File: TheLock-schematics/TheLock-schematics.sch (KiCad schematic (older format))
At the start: 4 parts

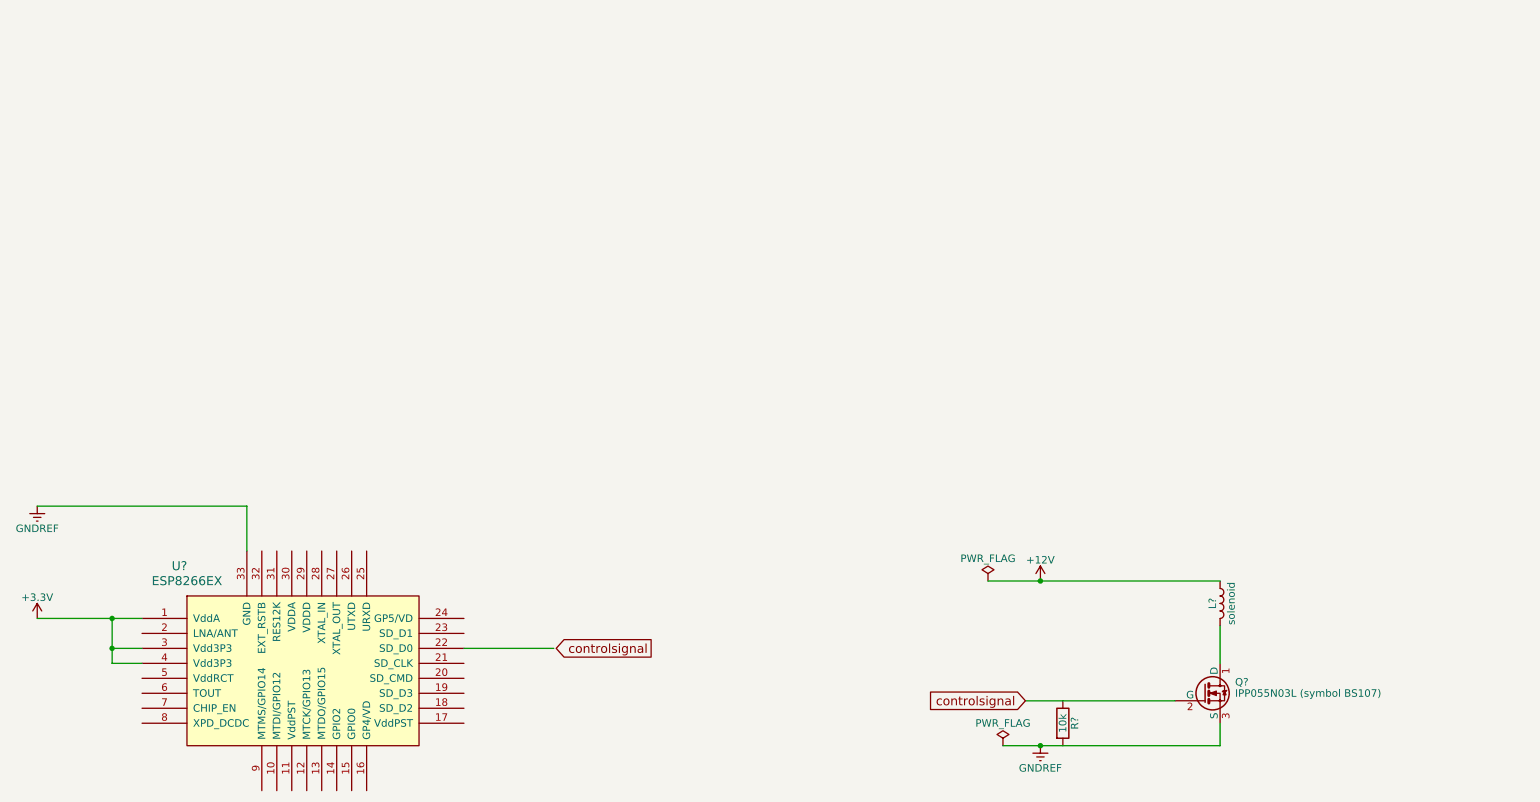
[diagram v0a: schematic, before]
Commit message: schematics: Add optical key sensor
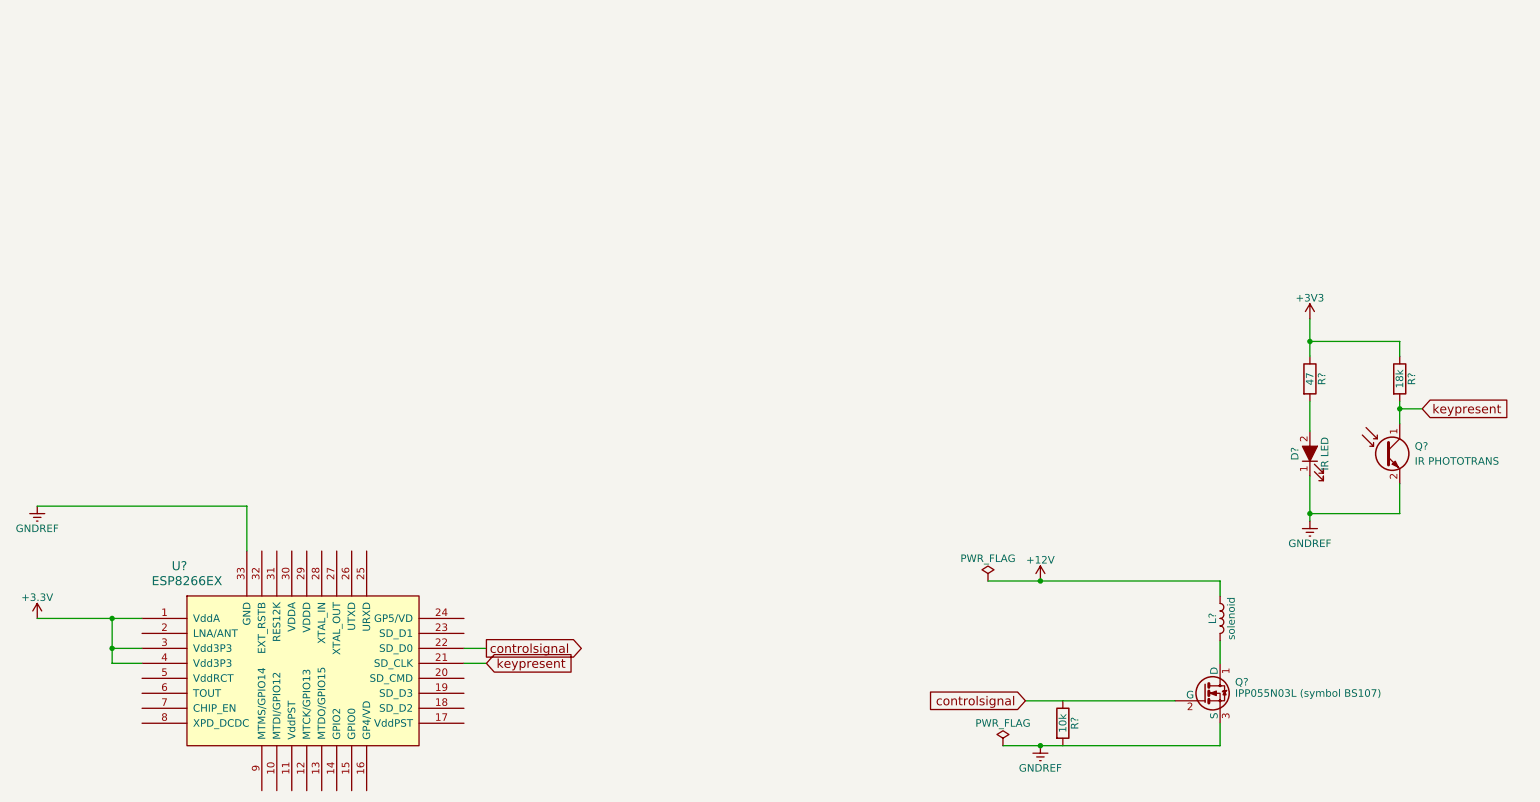
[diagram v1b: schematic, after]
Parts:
- added D?: IR LED, symbol LED_ALT
- added Q?: IR PHOTOTRANS, symbol Q_Photo_NPN
- added R?: 47, symbol R
- added R?: 18k, symbol R
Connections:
- net labels added: +3V3, keypresent
- wire segments 12 -> 31
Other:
- moved on the sheet: L?
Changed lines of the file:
@@
 LIBS:contrib
 LIBS:valves
-LIBS:ESP8266
 LIBS:TheLock-schematics-cache
 EELAYER 25 0
@@
 	9200 5700 9200 5550
 Wire Wire Line
-	7750 5700 9200 5700
+	7750 5700 8000 5700
+Wire Wire Line
+	8000 5700 9200 5700
 $Comp
 L L L?
 U 1 1 5957E9AE
-P 9200 4750
-F 0 "L?" V 9150 4750 50  0000 C CNN
-F 1 "solenoid" V 9275 4750 50  0000 C CNN
-F 2 "" H 9200 4750 50  0001 C CNN
-F 3 "" H 9200 4750 50  0001 C CNN
-	1    9200 4750
-	1    0    0    -1
-$EndComp
-Wire Wire Line
-	9200 5150 9200 4900
-Wire Wire Line
-	7650 4600 9200 4600
+P 9200 4850
+F 0 "L?" V 9150 4850 50  0000 C CNN
+F 1 "solenoid" V 9275 4850 50  0000 C CNN
+F 2 "" H 9200 4850 50  0001 C CNN
+F 3 "" H 9200 4850 50  0001 C CNN
+	1    9200 4850
+	1    0    0    -1
+$EndComp
+Wire Wire Line
+	9200 5150 9200 5000
+Wire Wire Line
+	7650 4600 8000 4600
+Wire Wire Line
+	8000 4600 9200 4600
 Text GLabel 7900 5400 0    60   Input ~ 0
 controlsignal
@@
 	1    0    0    -1
 $EndComp
-Text GLabel 5400 5050 0    60   Output ~ 0
+Text GLabel 4300 5050 2    60   Output ~ 0
 controlsignal
 Wire Wire Line
-	4750 5050 4150 5050
+	4300 5050 4150 5050
 $Comp
 L GNDREF #PWR?
@@
 $EndComp
 Wire Wire Line
-	1300 4850 2000 4850
+	1300 4850 1800 4850
+Wire Wire Line
+	1800 4850 2000 4850
 Wire Wire Line
 	2000 5050 1800 5050
 Wire Wire Line
-	1800 4850 1800 5150
+	1800 4850 1800 5050
+Wire Wire Line
+	1800 5050 1800 5150
 Connection ~ 1800 4850
 Wire Wire Line
 	1800 5150 2000 5150
 Connection ~ 1800 5050
+$Comp
+L LED_ALT D?
+U 1 1 595B8197
+P 9800 3750
+F 0 "D?" H 9800 3850 50  0000 C CNN
+F 1 "IR LED" H 9800 3650 50  0000 C CNN
+F 2 "" H 9800 3750 50  0001 C CNN
+F 3 "" H 9800 3750 50  0001 C CNN
+	1    9800 3750
+	0    -1   -1   0
+$EndComp
+$Comp
+L +3V3 #PWR?
+U 1 1 595B83C2
+P 9800 2850
+F 0 "#PWR?" H 9800 2700 50  0001 C CNN
+F 1 "+3V3" H 9800 2990 50  0000 C CNN
+F 2 "" H 9800 2850 50  0001 C CNN
+F 3 "" H 9800 2850 50  0001 C CNN
+	1    9800 2850
+	1    0    0    -1
+$EndComp
+$Comp
+L Q_Photo_NPN Q?
+U 1 1 595B83E5
+P 10300 3750
+F 0 "Q?" H 10500 3800 50  0000 L CNN
+F 1 "IR PHOTOTRANS" H 10500 3700 50  0000 L CNN
+F 2 "" H 10500 3850 50  0001 C CNN
+F 3 "" H 10300 3750 50  0001 C CNN
+	1    10300 3750
+	1    0    0    -1
+$EndComp
+Wire Wire Line
+	10400 4150 9800 4150
+$Comp
+L GNDREF #PWR?
+U 1 1 595B863D
+P 9800 4200
+F 0 "#PWR?" H 9800 3950 50  0001 C CNN
+F 1 "GNDREF" H 9800 4050 50  0000 C CNN
+F 2 "" H 9800 4200 50  0001 C CNN
+F 3 "" H 9800 4200 50  0001 C CNN
+	1    9800 4200
+	1    0    0    -1
+$EndComp
+Connection ~ 9800 4150
+Wire Wire Line
+	10400 4150 10400 3950
+Wire Wire Line
+	10400 3000 9800 3000
+Connection ~ 9800 3000
+$Comp
+L R R?
+U 1 1 595B89FB
+P 9800 3250
+F 0 "R?" V 9880 3250 50  0000 C CNN
+F 1 "47" V 9800 3250 50  0000 C CNN
+F 2 "" V 9730 3250 50  0001 C CNN
+F 3 "" H 9800 3250 50  0001 C CNN
+	1    9800 3250
+	1    0    0    -1
+$EndComp
+$Comp
+L R R?
+U 1 1 595B8B72
+P 10400 3250
+F 0 "R?" V 10480 3250 50  0000 C CNN
+F 1 "18k" V 10400 3250 50  0000 C CNN
+F 2 "" V 10330 3250 50  0001 C CNN
+F 3 "" H 10400 3250 50  0001 C CNN
+	1    10400 3250
+	1    0    0    -1
+$EndComp
+Wire Wire Line
+	10400 3100 10400 3000
+Wire Wire Line
+	10400 3400 10400 3450
+Wire Wire Line
+	10400 3450 10400 3550
+Wire Wire Line
+	9800 3400 9800 3600
+Wire Wire Line
+	9800 3900 9800 4150
+Wire Wire Line
+	9800 4150 9800 4200
+Wire Wire Line
+	9800 2850 9800 3000
+Wire Wire Line
+	9800 3000 9800 3100
+Text GLabel 10550 3450 2    60   Input ~ 0
+keypresent
+Wire Wire Line
+	10400 3450 10550 3450
+Connection ~ 10400 3450
+Wire Wire Line
+	9200 4600 9200 4700
+Text GLabel 4300 5150 2    60   Input ~ 0
+keypresent
+Wire Wire Line
+	4150 5150 4300 5150
+Wire Wire Line
+	4300 5150 4300 5150
 $EndSCHEMATC

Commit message: electronics: Update to the lock driver board
Will have header connectors, so that 3-4 of them
can be connected to a single ESP8266 module
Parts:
- removed L?: solenoid, symbol L
- removed U?: ESP8266EX, symbol ESP8266EX
- added D?: LED, symbol LED
- added J? (x2): Conn_01x04, symbol Conn_01x04
- added J?: Conn_01x02_Female, symbol Conn_01x02_Female
- added J?: Conn_01x02_Male, symbol Conn_01x02_Male
- added R?: R, symbol R
- Q?: value IPP055N03L (symbol BS107) -> IPP055N03L; footprint TO_SOT_Packages_THT:TO-92_Molded_Narrow -> TO_SOT_Packages_THT:TO-220_Horizontal; symbol BS107 -> BS107-RESCUE-TheLock-schematics
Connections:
- net controlsignal is gone; now on net unlock: Q?.2 (G)
- net +12V: now also J?.2 (Pin_2), J?.3 (Pin_3)
- net +3V3: now also J?.1 (Pin_1)
- net GNDREF: now also R?.2, D?.1 (K), J?.2 (Pin_2); no longer D?.1 (K)
- net keypresent: now also J?.2 (Pin_2)
- net solenoid-: now reaches Q?.1 (D)
- net solenoid-: now also J?.4 (Pin_4)
- net unlock: now reaches R?.1
- net unlock: now also J?.4 (Pin_4)
- net at D?.2 (A): now also J?.1 (Pin_1); no longer R?.2
- new net: D?.1 (K), J?.2 (Pin_2)
- new net: J?.1 (Pin_1), R?.2
- new net: D?.2 (A), R?.2
- new net GNDPWR: J?.1 (Pin_1)
- new net status: J?.3 (Pin_3), R?.1
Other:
- moved on the sheet: D?, Q?, R?

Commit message: electronics: Rough layout of lock board
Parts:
- D1: renamed from D?; footprint (none) -> LEDs:LED_0805_HandSoldering
- D2: renamed from D?; footprint (none) -> LEDs:LED_1206_HandSoldering
- J1: renamed from J?; value Conn_01x04 -> CONN_SIGNAL; footprint (none) -> Pin_Headers:Pin_Header_Angled_1x04_Pitch2.54mm
- J2: renamed from J?; value Conn_01x04 -> CONN_POWER; footprint (none) -> Pin_Headers:Pin_Header_Angled_1x04_Pitch2.54mm
- J3: renamed from J?; value Conn_01x02_Female -> CONN_IRBOARD; footprint (none) -> Socket_Strips:Socket_Strip_Angled_1x02_Pitch2.54mm
- J4: renamed from J?; value Conn_01x02_Male -> CONN_IRLED; footprint (none) -> Pin_Headers:Pin_Header_Angled_1x02_Pitch2.54mm
- Q1: renamed from Q?; value IPP055N03L -> PMV20XNE; footprint TO_SOT_Packages_THT:TO-220_Horizontal -> TO_SOT_Packages_SMD:SOT-23W_Handsoldering; symbol BS107-RESCUE-TheLock-schematics -> Q_NMOS_GSD
- Q2: renamed from Q?; footprint (none) -> Diodes_SMD:D_0805
- R1, R2, R3, R4: renamed from R?; footprint (none) -> Resistors_SMD:R_1210_HandSoldering
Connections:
- net GNDPWR: now also D2.1 (K), J3.2 (Pin_2), Q1.2 (S), Q2.2 (E), R1.2
- net solenoid-: now also Q1.3 (D); no longer Q1.1 (D)
- net unlock: now also Q1.1 (G); no longer Q1.2 (G)
- removed net GNDREF: D2.1 (K), J3.2 (Pin_2), Q1.3 (S), Q2.2 (E), R1.2
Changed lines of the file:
@@
 $EndDescr
 $Comp
-L GNDREF #PWR?
+L GNDREF #PWR01
 U 1 1 5957DA2E
 P 8700 3850
-F 0 "#PWR?" H 8700 3600 50  0001 C CNN
+F 0 "#PWR01" H 8700 3600 50  0001 C CNN
 F 1 "GNDREF" H 8700 3700 50  0000 C CNN
 F 2 "" H 8700 3850 50  0001 C CNN
@@
 $EndComp
 $Comp
-L +12V #PWR?
+L +12V #PWR02
 U 1 1 5957DA45
 P 8700 2800
-F 0 "#PWR?" H 8700 2650 50  0001 C CNN
+F 0 "#PWR02" H 8700 2650 50  0001 C CNN
 F 1 "+12V" H 8700 2940 50  0000 C CNN
 F 2 "" H 8700 2800 50  0001 C CNN
@@
 $EndComp
 $Comp
-L BS107-RESCUE-TheLock-schematics Q?
+L Q_NMOS_GSD Q1
 U 1 1 5957E897
 P 8600 3400
-F 0 "Q?" H 8800 3475 50  0000 L CNN
-F 1 "IPP055N03L" H 8800 3400 50  0000 L CNN
-F 2 "TO_SOT_Packages_THT:TO-220_Horizontal" H 8800 3325 50  0001 L CIN
+F 0 "Q1" H 8800 3475 50  0000 L CNN
+F 1 "PMV20XNE" H 8800 3400 50  0000 L CNN
+F 2 "TO_SOT_Packages_SMD:SOT-23W_Handsoldering" H 8800 3325 50  0001 L CIN
 F 3 "" H 8600 3400 50  0001 L CNN
 	1    8600 3400
@@
 Wire Wire Line
 	8700 3800 8700 3850
-Text GLabel 8150 3450 0    60   Input ~ 0
+Text GLabel 8050 3400 0    60   Input ~ 0
 unlock
 Wire Wire Line
-	8150 3450 8300 3450
-Wire Wire Line
-	8300 3450 8400 3450
-$Comp
-L R R?
+	8050 3400 8300 3400
+Wire Wire Line
+	8300 3400 8400 3400
+$Comp
+L R R1
 U 1 1 5957EABF
 P 8300 3650
-F 0 "R?" V 8380 3650 50  0000 C CNN
+F 0 "R1" V 8380 3650 50  0000 C CNN
 F 1 "10k" V 8300 3650 50  0000 C CNN
-F 2 "" V 8230 3650 50  0001 C CNN
+F 2 "Resistors_SMD:R_1210_HandSoldering" V 8230 3650 50  0001 C CNN
 F 3 "" H 8300 3650 50  0001 C CNN
 	1    8300 3650
@@
 $EndComp
 $Comp
-L LED_ALT D?
+L LED_ALT D1
 U 1 1 595B8197
 P 9650 1900
-F 0 "D?" H 9650 2000 50  0000 C CNN
+F 0 "D1" H 9650 2000 50  0000 C CNN
 F 1 "IR LED" H 9650 1800 50  0000 C CNN
-F 2 "" H 9650 1900 50  0001 C CNN
+F 2 "LEDs:LED_0805_HandSoldering" H 9650 1900 50  0001 C CNN
 F 3 "" H 9650 1900 50  0001 C CNN
 	1    9650 1900
@@
 $EndComp
 $Comp
-L +3V3 #PWR?
+L +3V3 #PWR03
 U 1 1 595B83C2
 P 8750 1000
-F 0 "#PWR?" H 8750 850 50  0001 C CNN
+F 0 "#PWR03" H 8750 850 50  0001 C CNN
 F 1 "+3V3" H 8750 1140 50  0000 C CNN
 F 2 "" H 8750 1000 50  0001 C CNN
@@
 $EndComp
 $Comp
-L Q_Photo_NPN Q?
+L Q_Photo_NPN Q2
 U 1 1 595B83E5
 P 10150 1900
-F 0 "Q?" H 10350 1950 50  0000 L CNN
+F 0 "Q2" H 10350 1950 50  0000 L CNN
 F 1 "IR PHOTOTRANS" H 10350 1850 50  0000 L CNN
-F 2 "" H 10350 2000 50  0001 C CNN
+F 2 "Diodes_SMD:D_0805" H 10350 2000 50  0001 C CNN
 F 3 "" H 10150 1900 50  0001 C CNN
 	1    10150 1900
@@
 $EndComp
 $Comp
-L GNDREF #PWR?
+L GNDREF #PWR04
 U 1 1 595B863D
 P 8750 2250
-F 0 "#PWR?" H 8750 2000 50  0001 C CNN
+F 0 "#PWR04" H 8750 2000 50  0001 C CNN
 F 1 "GNDREF" H 8750 2100 50  0000 C CNN
 F 2 "" H 8750 2250 50  0001 C CNN
@@
 	10250 2100 10250 2250
 $Comp
-L R R?
+L R R2
 U 1 1 595B89FB
 P 8750 1300
-F 0 "R?" V 8830 1300 50  0000 C CNN
+F 0 "R2" V 8830 1300 50  0000 C CNN
 F 1 "47" V 8750 1300 50  0000 C CNN
-F 2 "" V 8680 1300 50  0001 C CNN
+F 2 "Resistors_SMD:R_1210_HandSoldering" V 8680 1300 50  0001 C CNN
 F 3 "" H 8750 1300 50  0001 C CNN
 	1    8750 1300
@@
 $EndComp
 $Comp
-L R R?
+L R R3
 U 1 1 595B8B72
 P 10250 1300
-F 0 "R?" V 10330 1300 50  0000 C CNN
+F 0 "R3" V 10330 1300 50  0000 C CNN
 F 1 "18k" V 10250 1300 50  0000 C CNN
-F 2 "" V 10180 1300 50  0001 C CNN
+F 2 "Resistors_SMD:R_1210_HandSoldering" V 10180 1300 50  0001 C CNN
 F 3 "" H 10250 1300 50  0001 C CNN
 	1    10250 1300
@@
 Connection ~ 10250 1550
 $Comp
-L Conn_01x04 J?
+L Conn_01x04 J2
 U 1 1 59CF7CC0
 P 7650 2000
-F 0 "J?" H 7650 2300 50  0000 C CNN
-F 1 "Conn_01x04" H 7650 1700 50  0000 C CNN
-F 2 "" H 7650 2000 50  0001 C CNN
+F 0 "J2" H 7650 2300 50  0000 C CNN
+F 1 "CONN_POWER" H 7650 1700 50  0000 C CNN
+F 2 "Pin_Headers:Pin_Header_Angled_1x04_Pitch2.54mm" H 7650 2000 50  0001 C CNN
 F 3 "" H 7650 2000 50  0001 C CNN
 	1    7650 2000
@@
 $EndComp
 $Comp
-L +12V #PWR?
+L +12V #PWR05
 U 1 1 59CF7D47
 P 7100 2000
-F 0 "#PWR?" H 7100 1850 50  0001 C CNN
+F 0 "#PWR05" H 7100 1850 50  0001 C CNN
 F 1 "+12V" H 7100 2140 50  0000 C CNN
 F 2 "" H 7100 2000 50  0001 C CNN
@@
 $EndComp
 $Comp
-L GNDPWR #PWR?
+L GNDPWR #PWR06
 U 1 1 59CF7EAE
 P 6900 1900
-F 0 "#PWR?" H 6900 1700 50  0001 C CNN
+F 0 "#PWR06" H 6900 1700 50  0001 C CNN
 F 1 "GNDPWR" H 6900 1770 50  0000 C CNN
 F 2 "" H 6900 1850 50  0001 C CNN
@@
 $EndComp
 Wire Wire Line
-	6900 1900 7450 1900
+	6900 1900 7300 1900
+Wire Wire Line
+	7300 1900 7450 1900
 Wire Wire Line
 	8750 1850 8750 1450
 $Comp
-L +3.3V #PWR?
+L +3.3V #PWR07
 U 1 1 59D38CF5
 P 10250 1000
-F 0 "#PWR?" H 10250 850 50  0001 C CNN
+F 0 "#PWR07" H 10250 850 50  0001 C CNN
 F 1 "+3.3V" H 10250 1140 50  0000 C CNN
 F 2 "" H 10250 1000 50  0001 C CNN
@@
 $EndComp
 $Comp
-L GNDREF #PWR?
+L GNDREF #PWR08
 U 1 1 59D38D56
 P 10250 2250
-F 0 "#PWR?" H 10250 2000 50  0001 C CNN
+F 0 "#PWR08" H 10250 2000 50  0001 C CNN
 F 1 "GNDREF" H 10250 2100 50  0000 C CNN
 F 2 "" H 10250 2250 50  0001 C CNN
@@
 Connection ~ 8700 3800
 Wire Wire Line
-	8300 3500 8300 3450
-Connection ~ 8300 3450
+	8300 3500 8300 3400
+Connection ~ 8300 3400
 Wire Wire Line
 	8700 3150 8800 3150
@@
 	8750 1950 8850 1950
 $Comp
-L Conn_01x02_Female J?
+L Conn_01x02_Female J3
 U 1 1 59D39A33
 P 9050 1850
-F 0 "J?" H 9050 1950 50  0000 C CNN
-F 1 "Conn_01x02_Female" H 9150 1650 50  0000 C CNN
-F 2 "" H 9050 1850 50  0001 C CNN
+F 0 "J3" H 9050 1950 50  0000 C CNN
+F 1 "CONN_IRBOARD" H 9150 1650 50  0000 C CNN
+F 2 "Socket_Strips:Socket_Strip_Angled_1x02_Pitch2.54mm" H 9050 1850 50  0001 C CNN
 F 3 "" H 9050 1850 50  0001 C CNN
 	1    9050 1850
@@
 $EndComp
 $Comp
-L Conn_01x02_Male J?
+L Conn_01x02_Male J4
 U 1 1 59D39A82
 P 9150 1850
-F 0 "J?" H 9150 1950 50  0000 C CNN
-F 1 "Conn_01x02_Male" H 9150 2050 50  0000 C CNN
-F 2 "" H 9150 1850 50  0001 C CNN
+F 0 "J4" H 9150 1950 50  0000 C CNN
+F 1 "CONN_IRLED" H 9150 2050 50  0000 C CNN
+F 2 "Pin_Headers:Pin_Header_Angled_1x02_Pitch2.54mm" H 9150 1850 50  0001 C CNN
 F 3 "" H 9150 1850 50  0001 C CNN
 	1    9150 1850
@@
 unlock
 $Comp
-L +3V3 #PWR?
+L +3V3 #PWR09
 U 1 1 59D3AA96
 P 7050 1050
-F 0 "#PWR?" H 7050 900 50  0001 C CNN
+F 0 "#PWR09" H 7050 900 50  0001 C CNN
 F 1 "+3V3" H 7050 1190 50  0000 C CNN
 F 2 "" H 7050 1050 50  0001 C CNN
@@
 $EndComp
 $Comp
-L LED D?
+L LED D2
 U 1 1 59D3AB92
 P 10300 3550
-F 0 "D?" H 10300 3650 50  0000 C CNN
+F 0 "D2" H 10300 3650 50  0000 C CNN
 F 1 "LED" H 10300 3450 50  0000 C CNN
-F 2 "" H 10300 3550 50  0001 C CNN
+F 2 "LEDs:LED_1206_HandSoldering" H 10300 3550 50  0001 C CNN
 F 3 "" H 10300 3550 50  0001 C CNN
 	1    10300 3550
@@
 $EndComp
 $Comp
-L R R?
+L R R4
 U 1 1 59D3AC92
 P 10300 3200
-F 0 "R?" V 10380 3200 50  0000 C CNN
+F 0 "R4" V 10380 3200 50  0000 C CNN
 F 1 "R" V 10300 3200 50  0000 C CNN
-F 2 "" V 10230 3200 50  0001 C CNN
+F 2 "Resistors_SMD:R_1210_HandSoldering" V 10230 3200 50  0001 C CNN
 F 3 "" H 10300 3200 50  0001 C CNN
 	1    10300 3200
@@
 	10300 2900 10300 3050
 $Comp
-L GNDREF #PWR?
+L GNDREF #PWR010
 U 1 1 59D3ADAC
 P 10300 3800
-F 0 "#PWR?" H 10300 3550 50  0001 C CNN
+F 0 "#PWR010" H 10300 3550 50  0001 C CNN
 F 1 "GNDREF" H 10300 3650 50  0000 C CNN
 F 2 "" H 10300 3800 50  0001 C CNN
@@
 keypresent
 $Comp
-L Conn_01x04 J?
+L Conn_01x04 J1
 U 1 1 59D3B2F1
 P 7650 1150
-F 0 "J?" H 7650 1450 50  0000 C CNN
-F 1 "Conn_01x04" H 7650 850 50  0000 C CNN
-F 2 "" H 7650 1150 50  0001 C CNN
+F 0 "J1" H 7650 1450 50  0000 C CNN
+F 1 "CONN_SIGNAL" H 7650 850 50  0000 C CNN
+F 2 "Pin_Headers:Pin_Header_Angled_1x04_Pitch2.54mm" H 7650 1150 50  0001 C CNN
 F 3 "" H 7650 1150 50  0001 C CNN
 	1    7650 1150
@@
 Wire Wire Line
 	7300 2100 7450 2100
+$Comp
+L GNDREF #PWR?
+U 1 1 59D3C19C
+P 7150 1750
+F 0 "#PWR?" H 7150 1500 50  0001 C CNN
+F 1 "GNDREF" H 7150 1600 50  0000 C CNN
+F 2 "" H 7150 1750 50  0001 C CNN
+F 3 "" H 7150 1750 50  0001 C CNN
+	1    7150 1750
+	0    1    1    0
+$EndComp
+Wire Wire Line
+	7150 1750 7300 1750
+Wire Wire Line
+	7300 1750 7300 1900
+Connection ~ 7300 1900
 $EndSCHEMATC

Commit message: electronics: PCB layout and mechanics should conform now
IR phototrans and LED should be positioned OK
PCB size and attachment should be roughly OK
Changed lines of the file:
@@
 $EndComp
 Wire Wire Line
-	8700 3600 8700 3800
-Wire Wire Line
-	8700 3800 8700 3850
+	8700 3600 8700 3850
 Text GLabel 8050 3400 0    60   Input ~ 0
 unlock
 Wire Wire Line
-	8050 3400 8300 3400
-Wire Wire Line
-	8300 3400 8400 3400
+	8050 3400 8400 3400
 $Comp
 L R R1
@@
 	10250 1000 10250 1150
 Wire Wire Line
-	10250 1450 10250 1550
-Wire Wire Line
-	10250 1550 10250 1700
+	10250 1450 10250 1700
 Wire Wire Line
 	8750 1950 8750 2250
@@
 $EndComp
 Wire Wire Line
-	6900 1900 7300 1900
-Wire Wire Line
-	7300 1900 7450 1900
+	6900 1900 7450 1900
 Wire Wire Line
 	8750 1850 8750 1450
@@
 	7300 2100 7450 2100
 $Comp
-L GNDREF #PWR?
+L GNDREF #PWR011
 U 1 1 59D3C19C
 P 7150 1750
-F 0 "#PWR?" H 7150 1500 50  0001 C CNN
+F 0 "#PWR011" H 7150 1500 50  0001 C CNN
 F 1 "GNDREF" H 7150 1600 50  0000 C CNN
 F 2 "" H 7150 1750 50  0001 C CNN
